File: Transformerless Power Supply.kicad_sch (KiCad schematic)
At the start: 18 parts, among them J1 Screw_Terminal_01x02, J2 Screw_Terminal_01x02, U1 LM7805_TO220

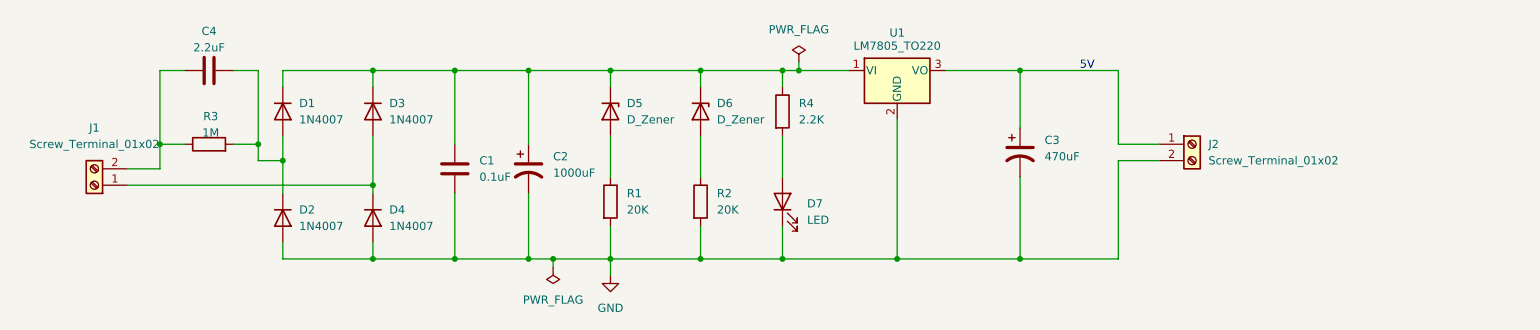
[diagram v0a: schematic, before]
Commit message: Schematic with Footprints Assigned
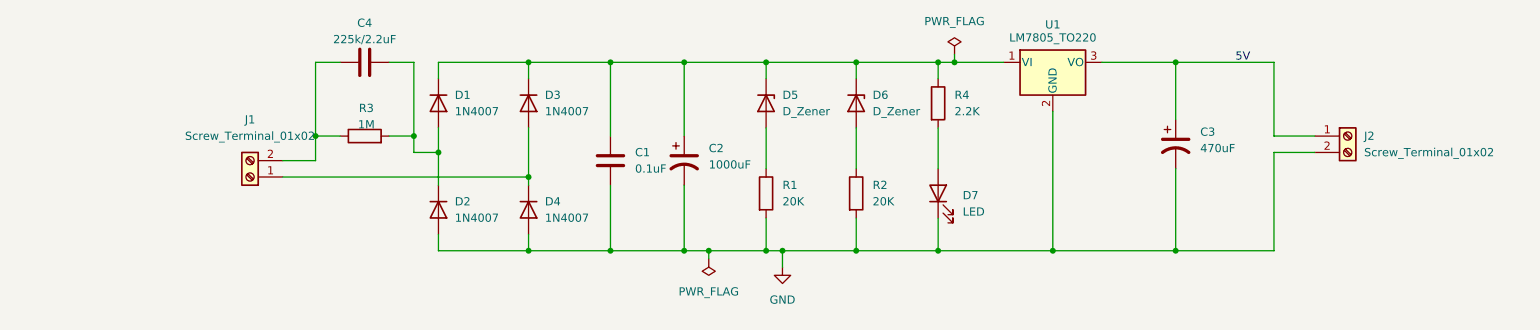
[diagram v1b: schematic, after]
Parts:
- C1: footprint (none) -> Capacitor_THT:C_Disc_D4.7mm_W2.5mm_P5.00mm
- C2: footprint (none) -> Capacitor_THT:CP_Radial_D10.0mm_P5.00mm
- C3: footprint (none) -> Capacitor_THT:CP_Radial_D10.0mm_P3.80mm
- C4: value 2.2uF -> 225k/2.2uF; footprint (none) -> Capacitor_THT:C_Rect_L18.0mm_W6.0mm_P15.00mm_FKS3_FKP3
- D5, D6: footprint (none) -> Diode_THT:D_A-405_P7.62mm_Horizontal
- D7: footprint (none) -> LED_THT:LED_D5.0mm
- J1, J2: footprint (none) -> TerminalBlock:TerminalBlock_bornier-2_P5.08mm
- R1, R2, R3, R4: footprint (none) -> Resistor_THT:R_Axial_DIN0207_L6.3mm_D2.5mm_P7.62mm_Horizontal
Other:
- title: (none) -> Transformerless Power Supply Project
- moved on the sheet: C1, C2, C3, C4, D1, D2, D3, D4, D5, D6, D7, J1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
